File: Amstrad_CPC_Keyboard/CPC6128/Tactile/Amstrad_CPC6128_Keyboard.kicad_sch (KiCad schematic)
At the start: 85 parts, among them J1 POWER, SW1 DEL, SW10 FOUR, SW11 THREE, SW12 E, SW13 W, SW14 S, SW15 D, SW16 C, SW17 X, SW18 SIX, SW19 FIVE, SW2 ONE, SW20 R, SW21 T, SW22 G, SW23 F, SW24 B, SW25 V, SW26 EIGHT, SW27 ZERO, SW28 ^CARAT^, SW29 SEVEN, SW3 TWO, SW30 NINE, SW31 -MINUS-, SW32 U, SW33 O, SW34 @AT@, SW35 Y, SW36 I, SW37 P, SW38 H, SW39 L, SW4 ESC, SW40 ;SEMI_COLON;, SW41 J, SW42 K, SW43 :COLON:, SW44 N, SW45 M, SW46 /FORWSLASH/, SW47 SPACE, SW48 ,COMMA,, SW49 .DOT., SW5 Q, SW50 CLR, SW51 LEFT, SW52 UP, SW53 [, SW54 COPY, SW55 RIGHT, SW56 ENTER, SW57 NP_SEVEN, SW58 DOWN, SW59 ], SW6 TAB, SW60 NP_EIGHT, SW61 NP_NINE, SW62 NP_FOUR, SW63 NP_FIVE, SW64 NP_SIX, SW65 LH_SHIFT, SW66 NP_ONE, SW67 NP_THREE, SW68 \BACKSLASH\, SW69 NP_TWO, SW7 A, SW70 NP_ENTER, SW71 CTRL, SW72 NP_ZERO, SW73 NP_DOT, SW74 RH_SHIFT, SW75 SW_SPST, SW8 CAPS_LOCK, SW9 Z

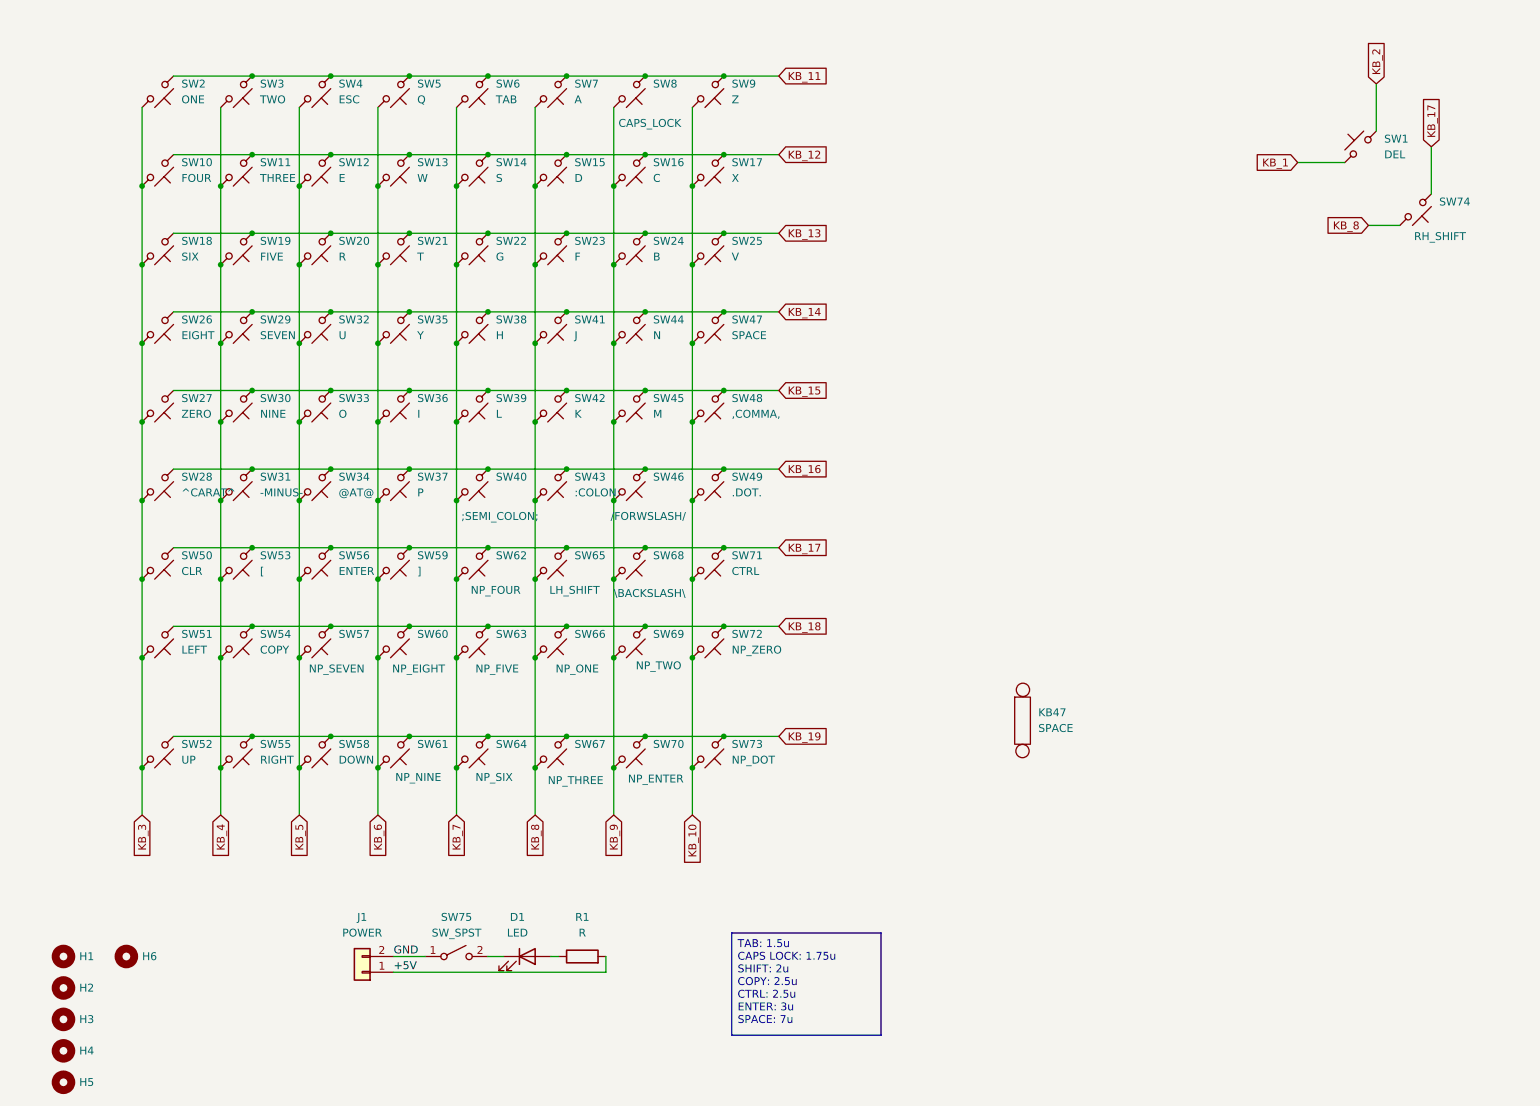
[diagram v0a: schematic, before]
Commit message: Finalising 12mm tactile design
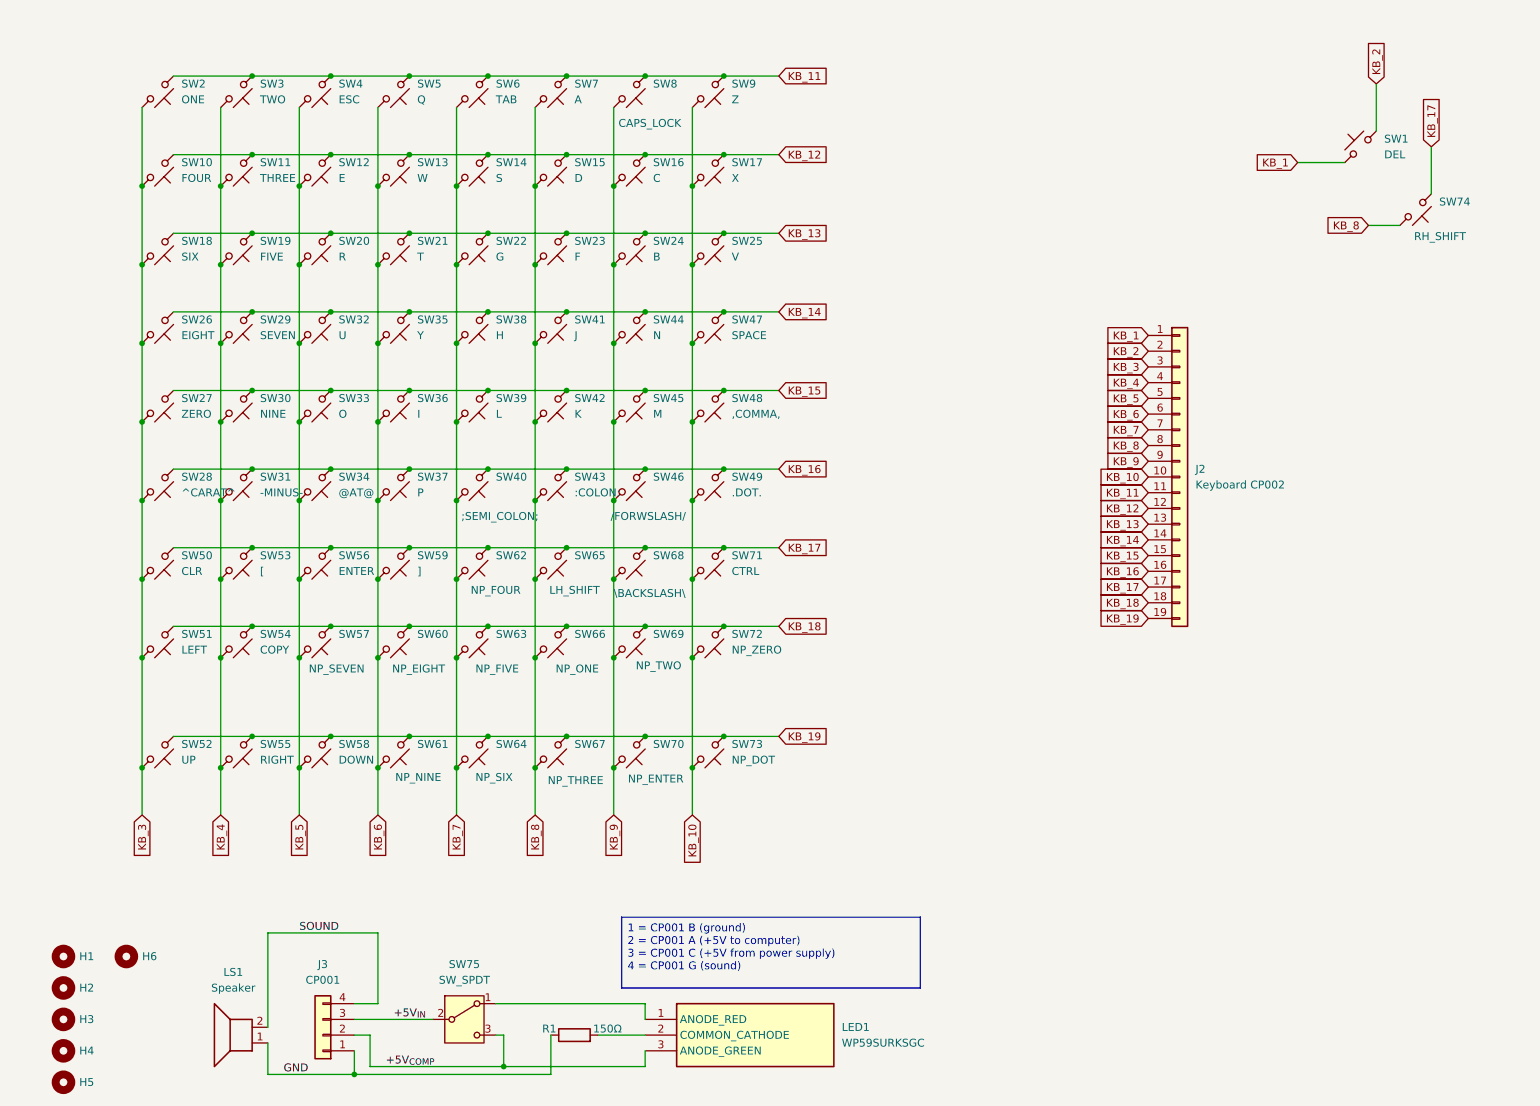
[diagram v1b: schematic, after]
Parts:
- removed D1: LED, LED_THT:LED_D5.0mm, symbol Device:LED
- removed J1: POWER, Connector_PinHeader_2.54mm:PinHeader_1x02_P2.54mm_Vertical, symbol Connector_Generic:Conn_01x02
- removed KB47: SPACE, PCM_Mounting_Keyboard_Stabilizer:Stabilizer_Cherry_MX_7.00u, symbol Clueless_Engineer:Stabiliser
- removed SW75: SW_SPST, Button_Switch_THT:SW_Slide_SPDT_Straight_CK_OS102011MS2Q, symbol Switch:SW_SPST
- added J2: Keyboard CP002, Connector_PinHeader_2.54mm:PinHeader_1x19_P2.54mm_Vertical, symbol Connector_Generic:Conn_01x19
- added J3: CP001, Connector_PinHeader_2.54mm:PinHeader_1x04_P2.54mm_Vertical, symbol Connector_Generic:Conn_01x04
- added LED1: WP59SURKSGC, LED_THT:WP59EGC, symbol LED:WP59SURKSGC
- added LS1: Speaker, Buzzer_Beeper:Buzzer_12x9.5RM7.6, symbol Device:Speaker
- added SW75: SW_SPDT, Button_Switch_THT:L102011MS02Q, symbol Switch:SW_SPDT
- R1: value R -> 150Ω
- SW1, SW10, SW11, SW12, SW13, SW14, SW15, SW16, SW17, SW18, SW19, SW2, SW20, SW21, SW22, SW23, SW24, SW25, SW26, SW27, SW28, SW29, SW3, SW30, SW31, SW32, SW33, SW34, SW35, SW36, SW37, SW38, SW39, SW4, SW40, SW41, SW42, SW43, SW44, SW45, SW46, SW48, SW49, SW5, SW50, SW51, SW52, SW53, SW55, SW57, SW58, SW59, SW60, SW61, SW62, SW63, SW64, SW66, SW67, SW68, SW69, SW7, SW72, SW73, SW9: footprint PCM_Switch_Keyboard_Cherry_MX:SW_Cherry_MX_PCB_1.00u -> Button_Switch_THT:SW_PUSH-12mm
- SW47: footprint PCM_Switch_Keyboard_Cherry_MX:SW_Cherry_MX_PCB_7.00u -> Button_Switch_THT:SW_PUSH-12mm
- SW54, SW71: footprint PCM_Switch_Keyboard_Cherry_MX:SW_Cherry_MX_PCB_2.50u -> Button_Switch_THT:SW_PUSH-12mm
- SW56: footprint PCM_Switch_Keyboard_Cherry_MX:SW_Cherry_MX_PCB_ISOEnter -> Button_Switch_THT:SW_PUSH-12mm
- SW6: footprint PCM_Switch_Keyboard_Cherry_MX:SW_Cherry_MX_PCB_1.50u -> Button_Switch_THT:SW_PUSH-12mm
- SW65, SW74: footprint PCM_Switch_Keyboard_Cherry_MX:SW_Cherry_MX_PCB_2.00u -> Button_Switch_THT:SW_PUSH-12mm
- SW70: footprint PCM_Switch_Keyboard_Cherry_MX:SW_Cherry_MX_PCB_3.00u -> Button_Switch_THT:SW_PUSH-12mm
- SW8: footprint PCM_Switch_Keyboard_Cherry_MX:SW_Cherry_MX_PCB_1.75u -> Button_Switch_THT:SW_PUSH-12mm
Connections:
- net GND: now also R1.1, J3.1 (Pin_1), LS1.1
- net KB_1: now also J2.1 (Pin_1)
- net KB_10: now also J2.10 (Pin_10)
- net KB_11: now also J2.11 (Pin_11)
- net KB_12: now also J2.12 (Pin_12)
- net KB_13: now also J2.13 (Pin_13)
- net KB_14: now also J2.14 (Pin_14)
- net KB_15: now also J2.15 (Pin_15)
- net KB_16: now also J2.16 (Pin_16)
- net KB_17: now also J2.17 (Pin_17)
- net KB_18: now also J2.18 (Pin_18)
- net KB_19: now also J2.19 (Pin_19)
- net KB_2: now also J2.2 (Pin_2)
- net KB_3: now also J2.3 (Pin_3)
- net KB_4: now also J2.4 (Pin_4)
- net KB_5: now also J2.5 (Pin_5)
- net KB_6: now also J2.6 (Pin_6)
- net KB_7: now also J2.7 (Pin_7)
- net KB_8: now also J2.8 (Pin_8)
- net KB_9: now also J2.9 (Pin_9)
- net +5V: no longer names the net of R1.2
- net +5V: now also LED1.2 (COMMON_CATHODE)
- new net: LED1.1 (ANODE_RED), SW75.1 (A)
- new net +5V_{COMP}: J3.2 (Pin_2), LED1.3 (ANODE_GREEN), SW75.3 (C)
- new net +5V_{IN}: J3.3 (Pin_3), SW75.2 (B)
- new net SOUND: J3.4 (Pin_4), LS1.2
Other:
- company: (none) -> Brett Hallen
- title: (none) -> Amstrad CPC Troubleshooting Keyboard (Tactile)
- moved on the sheet: R1

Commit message: Finalised Rev. A of tactile keyboard design
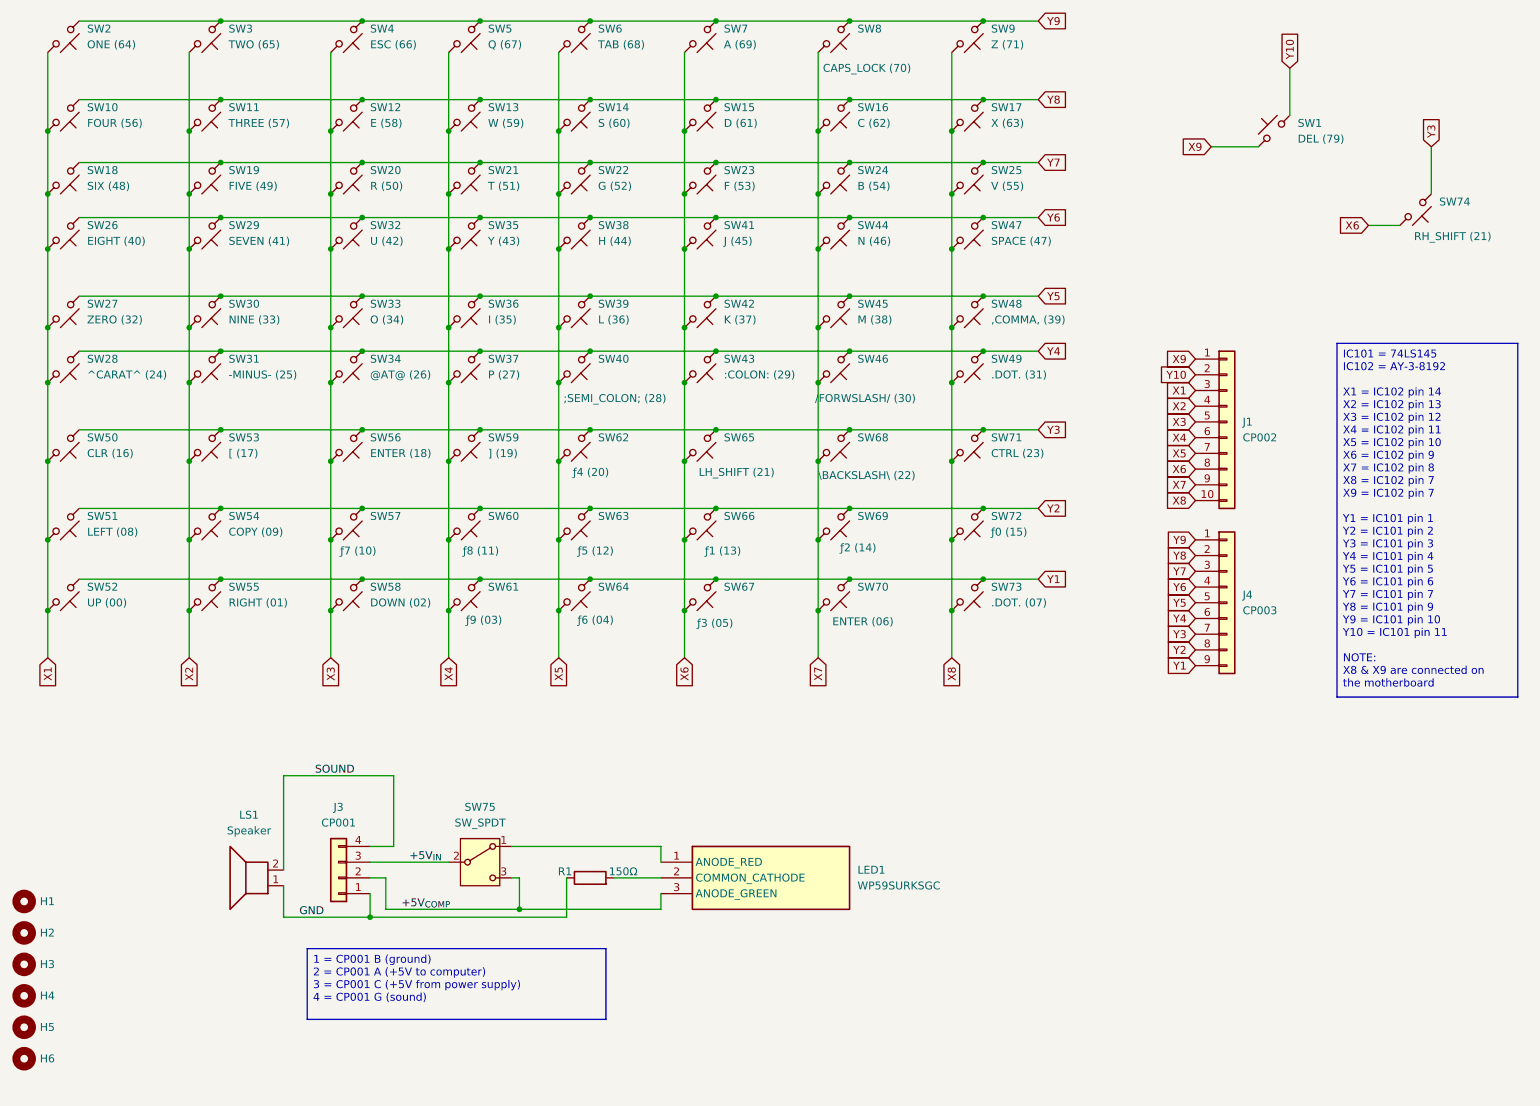
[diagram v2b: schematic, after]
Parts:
- removed J2: Keyboard CP002, Connector_PinHeader_2.54mm:PinHeader_1x19_P2.54mm_Vertical, symbol Connector_Generic:Conn_01x19
- added J1: CP002, Connector_PinHeader_2.54mm:PinHeader_1x10_P2.54mm_Vertical, symbol Connector_Generic:Conn_01x10
- added J4: CP003, Connector_PinHeader_2.54mm:PinHeader_1x09_P2.54mm_Vertical, symbol Connector_Generic:Conn_01x09
- SW1: value DEL -> DEL (79)
- SW10: value FOUR -> FOUR (56)
- SW11: value THREE -> THREE (57)
- SW12: value E -> E (58)
- SW13: value W -> W (59)
- SW14: value S -> S (60)
- SW15: value D -> D (61)
- SW16: value C -> C (62)
- SW17: value X -> X (63)
- SW18: value SIX -> SIX (48)
- SW19: value FIVE -> FIVE (49)
- SW2: value ONE -> ONE (64)
- SW20: value R -> R (50)
- SW21: value T -> T (51)
- SW22: value G -> G (52)
- SW23: value F -> F (53)
- SW24: value B -> B (54)
- SW25: value V -> V (55)
- SW26: value EIGHT -> EIGHT (40)
- SW27: value ZERO -> ZERO (32)
- SW28: value ^CARAT^ -> ^CARAT^ (24)
- SW29: value SEVEN -> SEVEN (41)
- SW3: value TWO -> TWO (65)
- SW30: value NINE -> NINE (33)
- SW31: value -MINUS- -> -MINUS- (25)
- SW32: value U -> U (42)
- SW33: value O -> O (34)
- SW34: value @AT@ -> @AT@ (26)
- SW35: value Y -> Y (43)
- SW36: value I -> I (35)
- SW37: value P -> P (27)
- SW38: value H -> H (44)
- SW39: value L -> L (36)
- SW4: value ESC -> ESC (66)
- SW40: value ;SEMI_COLON; -> ;SEMI_COLON; (28)
- SW41: value J -> J (45)
- SW42: value K -> K (37)
- SW43: value :COLON: -> :COLON: (29)
- SW44: value N -> N (46)
- SW45: value M -> M (38)
- SW46: value /FORWSLASH/ -> /FORWSLASH/ (30)
- SW47: value SPACE -> SPACE (47)
- SW48: value ,COMMA, -> ,COMMA, (39)
- SW49: value .DOT. -> .DOT. (31)
- SW5: value Q -> Q (67)
- SW50: value CLR -> CLR (16)
- SW51: value LEFT -> LEFT (08)
- SW52: value UP -> UP (00)
- SW53: value [ -> [ (17)
- SW54: value COPY -> COPY (09)
- SW55: value RIGHT -> RIGHT (01)
- SW56: value ENTER -> ENTER (18)
- SW57: value NP_SEVEN -> ƒ7 (10)
- SW58: value DOWN -> DOWN (02)
- SW59: value ] -> ] (19)
- SW6: value TAB -> TAB (68)
- SW60: value NP_EIGHT -> ƒ8 (11)
- SW61: value NP_NINE -> ƒ9 (03)
- SW62: value NP_FOUR -> ƒ4 (20)
- SW63: value NP_FIVE -> ƒ5 (12)
- SW64: value NP_SIX -> ƒ6 (04)
- SW65: value LH_SHIFT -> LH_SHIFT (21)
- SW66: value NP_ONE -> ƒ1 (13)
- SW67: value NP_THREE -> ƒ3 (05)
- SW68: value \BACKSLASH\ -> \BACKSLASH\ (22)
- SW69: value NP_TWO -> ƒ2 (14)
- SW7: value A -> A (69)
- SW70: value NP_ENTER -> ENTER (06)
- SW71: value CTRL -> CTRL (23)
- SW72: value NP_ZERO -> ƒ0 (15)
- SW73: value NP_DOT -> .DOT. (07)
- SW74: value RH_SHIFT -> RH_SHIFT (21)
- SW8: value CAPS_LOCK -> CAPS_LOCK (70)
- SW9: value Z -> Z (71)
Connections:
- net KB_1 renamed X9
- net X9: now also J1.1 (Pin_1)
- net KB_10 renamed X8
- net X8: now also J1.10 (Pin_10)
- net KB_11 renamed Y9
- net Y9: now also J4.1 (Pin_1)
- net KB_12 renamed Y8
- net Y8: now also J4.2 (Pin_2)
- net KB_13 renamed Y7
- net Y7: now also J4.3 (Pin_3)
- net KB_14 renamed Y6
- net Y6: now also J4.4 (Pin_4)
- net KB_15 renamed Y5
- net Y5: now also J4.5 (Pin_5)
- net KB_16 renamed Y4
- net Y4: now also J4.6 (Pin_6)
- net KB_17 renamed Y3
- net Y3: now also J4.7 (Pin_7)
- net KB_18 renamed Y2
- net Y2: now also J4.8 (Pin_8)
- net KB_19 renamed Y1
- net Y1: now also J4.9 (Pin_9)
- net KB_2 renamed Y10
- net Y10: now also J1.2 (Pin_2)
- net KB_3 renamed X1
- net X1: now also J1.3 (Pin_3)
- net KB_4 renamed X2
- net X2: now also J1.4 (Pin_4)
- net KB_5 renamed X3
- net X3: now also J1.5 (Pin_5)
- net KB_6 renamed X4
- net X4: now also J1.6 (Pin_6)
- net KB_7 renamed X5
- net X5: now also J1.7 (Pin_7)
- net KB_8 renamed X6
- net X6: now also J1.8 (Pin_8)
- net KB_9 renamed X7
- net X7: now also J1.9 (Pin_9)
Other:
- moved on the sheet: H1, H2, H3, H4, H5, H6, J3, LED1, LS1, R1, SW1, SW10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
